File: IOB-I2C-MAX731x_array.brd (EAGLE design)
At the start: 108.7 x 112 mm, 30 parts, among them IC1X11 MAX7311, IC1X12 MAX7311, IC1X13 MAX7311, SW1X11 A0, SW1X12 A0, SW1X13 A0, SW2X11 A1, SW2X12 A1, SW2X13 A1, SW3X11 A2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

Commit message: cleanup layout
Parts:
- BOARDX11, BOARDX12, BOARDX13: value I2C-EXPANDER -> CONNECTOR-I2C-EXPANDER
- moved U$1X13 2.84 mm to (19.7, 75.1)
- moved U$1X11 2.84 mm to (19.7, 9.02)
- moved U$1X12 2.84 mm to (19.7, 42.0)
- moved IC1X12 1.27 mm to (48.3, 52.1)
- moved SW1X12 1.27 mm to (73.0, 41.9)
- moved SW2X12 1.27 mm to (54.0, 41.9)
- moved SW3X12 1.27 mm to (34.9, 41.9)
- moved IC1X11 1.27 mm to (48.3, 19.1)
- moved SW1X11 1.27 mm to (73.0, 8.89)
- moved SW2X11 1.27 mm to (54.0, 8.89)
- moved SW3X11 1.27 mm to (34.9, 8.89)
- moved IC1X13 1.27 mm to (48.3, 85.1)
- moved SW1X13 1.27 mm to (73.0, 74.9)
- moved SW2X13 1.27 mm to (54.0, 74.9)
- moved SW3X13 1.27 mm to (34.9, 74.9)
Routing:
- net VCCX13: track 10.8 -> 0.00 mm, vias 2 -> 0
- net VCCX12: track 10.8 -> 0.00 mm, vias 2 -> 0
- net VCCX11: track 10.8 -> 0.00 mm, vias 2 -> 0
- net P9X13: track 31.2 -> 32.5 mm
- net P8X13: track 31.5 -> 32.8 mm
- net P9X12: track 31.2 -> 32.5 mm
- net P7X11: track 29.6 -> 30.9 mm
- net P8X12: track 31.5 -> 32.8 mm
- net P11X11: track 24.5 -> 25.8 mm
- net P10X12: track 29.7 -> 31.0 mm
- net P8X11: track 31.5 -> 32.8 mm
- net P6X11: track 25.2 -> 26.4 mm
- net P5X11: track 23.7 -> 24.9 mm
- net P12X11: track 22.6 -> 23.9 mm
- net P10X11: track 29.7 -> 31.0 mm
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
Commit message: added values for connectors
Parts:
- FID-LR, FID-UL: value (none) -> FIDUCIAL
- U$5X1: value (none) -> 10x10
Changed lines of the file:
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@@
 <element name="SW3X13" library="SPCoast" package="EDG-04" value="A2" x="34.925" y="74.93" rot="R180"/>
 <element name="U$1X13" library="SPCoast" package="OSHW-LOGO-L" value="DOC-OSHW-LOGO-L" x="19.685" y="75.057"/>
-<element name="FID-LR" library="SPCoast" package="FIDUCIAL_1MM" value="" x="93.98" y="8.89"/>
-<element name="FID-UL" library="SPCoast" package="FIDUCIAL_1MM" value="" x="5.08" y="91.44" smashed="yes">
+<element name="FID-LR" library="SPCoast" package="FIDUCIAL_1MM" value="FIDUCIAL" x="93.98" y="8.89"/>
+<element name="FID-UL" library="SPCoast" package="FIDUCIAL_1MM" value="FIDUCIAL" x="5.08" y="91.44" smashed="yes">
 <attribute name="NAME" x="8.255" y="88.9" size="1.016" layer="25" rot="R180"/>
 </element>
-<element name="U$5X1" library="SPCoast" package="BOARD-TEMPLATE-IOB-I2C-3X1-ARRAY" value="" x="0" y="0"/>
+<element name="U$5X1" library="SPCoast" package="BOARD-TEMPLATE-IOB-I2C-3X1-ARRAY" value="10x10" x="0" y="0"/>
 </elements>
 <signals>

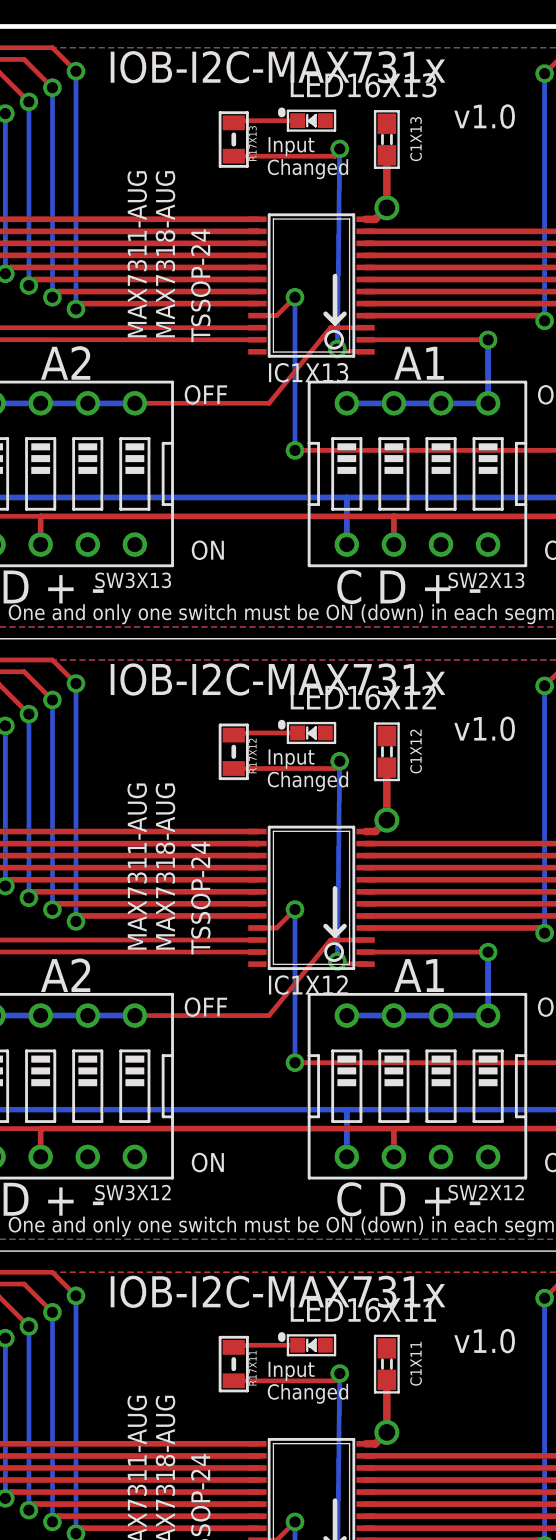
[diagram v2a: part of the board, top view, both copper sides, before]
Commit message: normalized values
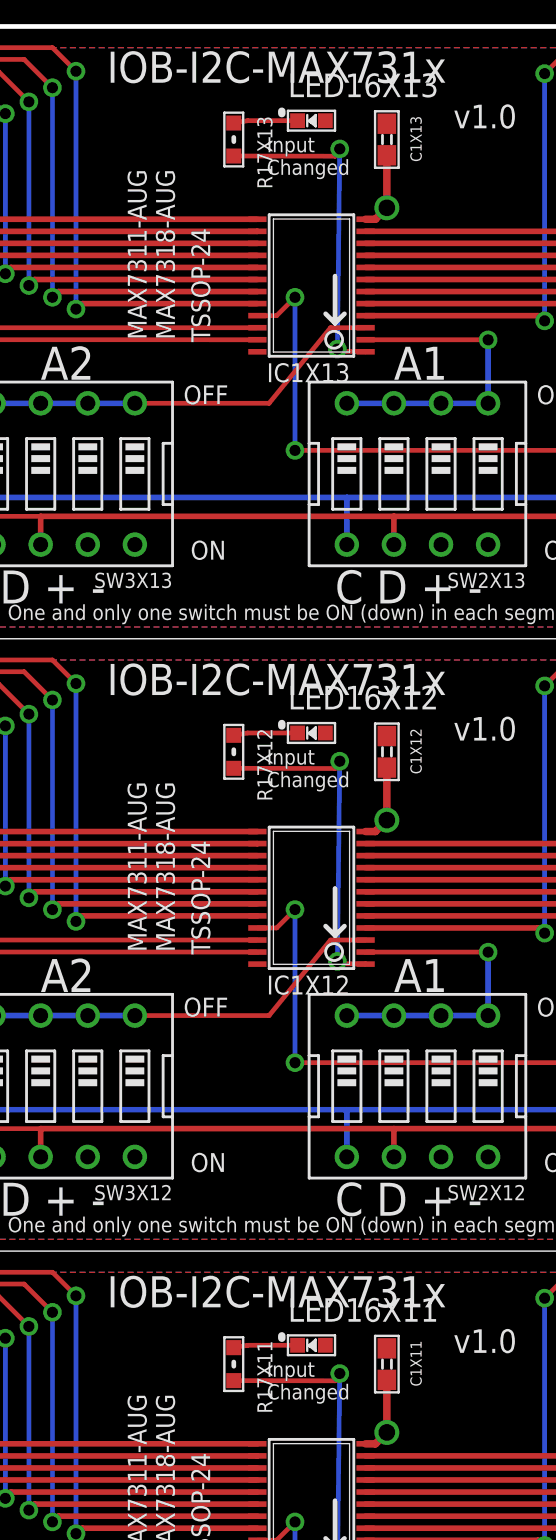
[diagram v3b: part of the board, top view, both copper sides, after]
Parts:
- R17X11, R17X12, R17X13: device SPCoast:0805-RES -> SPCoast:0603-RES
- SW1X11, SW1X12, SW1X13: value A0 -> SPSTx4
- SW2X11, SW2X12, SW2X13: value A1 -> SPSTx4
- SW3X11, SW3X12, SW3X13: value A2 -> SPSTx4
- U$5X1: value 10x10 -> BOARD
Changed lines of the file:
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@@
 <element name="IC1X11" library="SPCoast" package="TSSOP24" value="MAX7311" x="48.26" y="19.05" rot="R90"/>
 <element name="LED16X11" library="SPCoast" package="0603-LED" value="G" x="48.26" y="27.94"/>
-<element name="R17X11" library="SPCoast" package="0805-RES" value="4k7" x="44.069" y="26.924" rot="R270"/>
-<element name="SW1X11" library="SPCoast" package="EDG-04" value="A0" x="73.025" y="8.89" rot="R180"/>
-<element name="SW2X11" library="SPCoast" package="EDG-04" value="A1" x="53.975" y="8.89" rot="R180"/>
-<element name="SW3X11" library="SPCoast" package="EDG-04" value="A2" x="34.925" y="8.89" rot="R180"/>
+<element name="R17X11" library="SPCoast" package="0603-RES" value="4k7" x="44.069" y="26.924" rot="R270"/>
+<element name="SW1X11" library="SPCoast" package="EDG-04" value="SPSTx4" x="73.025" y="8.89" rot="R180"/>
+<element name="SW2X11" library="SPCoast" package="EDG-04" value="SPSTx4" x="53.975" y="8.89" rot="R180"/>
+<element name="SW3X11" library="SPCoast" package="EDG-04" value="SPSTx4" x="34.925" y="8.89" rot="R180"/>
 <element name="U$1X11" library="SPCoast" package="OSHW-LOGO-L" value="DOC-OSHW-LOGO-L" x="19.685" y="9.017"/>
 <element name="BOARDX12" library="SPCoast" package="I2C-EXPANDER" value="CONNECTOR-I2C-EXPANDER" x="48.26" y="60.96"/>
@@
 <element name="IC1X12" library="SPCoast" package="TSSOP24" value="MAX7311" x="48.26" y="52.07" rot="R90"/>
 <element name="LED16X12" library="SPCoast" package="0603-LED" value="G" x="48.26" y="60.96"/>
-<element name="R17X12" library="SPCoast" package="0805-RES" value="4k7" x="44.069" y="59.944" rot="R270"/>
-<element name="SW1X12" library="SPCoast" package="EDG-04" value="A0" x="73.025" y="41.91" rot="R180"/>
-<element name="SW2X12" library="SPCoast" package="EDG-04" value="A1" x="53.975" y="41.91" rot="R180"/>
-<element name="SW3X12" library="SPCoast" package="EDG-04" value="A2" x="34.925" y="41.91" rot="R180"/>
+<element name="R17X12" library="SPCoast" package="0603-RES" value="4k7" x="44.069" y="59.944" rot="R270"/>
+<element name="SW1X12" library="SPCoast" package="EDG-04" value="SPSTx4" x="73.025" y="41.91" rot="R180"/>
+<element name="SW2X12" library="SPCoast" package="EDG-04" value="SPSTx4" x="53.975" y="41.91" rot="R180"/>
+<element name="SW3X12" library="SPCoast" package="EDG-04" value="SPSTx4" x="34.925" y="41.91" rot="R180"/>
 <element name="U$1X12" library="SPCoast" package="OSHW-LOGO-L" value="DOC-OSHW-LOGO-L" x="19.685" y="42.037"/>
 <element name="BOARDX13" library="SPCoast" package="I2C-EXPANDER" value="CONNECTOR-I2C-EXPANDER" x="48.26" y="93.98"/>
@@
 <element name="IC1X13" library="SPCoast" package="TSSOP24" value="MAX7311" x="48.26" y="85.09" rot="R90"/>
 <element name="LED16X13" library="SPCoast" package="0603-LED" value="G" x="48.26" y="93.98"/>
-<element name="R17X13" library="SPCoast" package="0805-RES" value="4k7" x="44.069" y="92.964" rot="R270"/>
-<element name="SW1X13" library="SPCoast" package="EDG-04" value="A0" x="73.025" y="74.93" rot="R180"/>
-<element name="SW2X13" library="SPCoast" package="EDG-04" value="A1" x="53.975" y="74.93" rot="R180"/>
-<element name="SW3X13" library="SPCoast" package="EDG-04" value="A2" x="34.925" y="74.93" rot="R180"/>
+<element name="R17X13" library="SPCoast" package="0603-RES" value="4k7" x="44.069" y="92.964" rot="R270"/>
+<element name="SW1X13" library="SPCoast" package="EDG-04" value="SPSTx4" x="73.025" y="74.93" rot="R180"/>
+<element name="SW2X13" library="SPCoast" package="EDG-04" value="SPSTx4" x="53.975" y="74.93" rot="R180"/>
+<element name="SW3X13" library="SPCoast" package="EDG-04" value="SPSTx4" x="34.925" y="74.93" rot="R180"/>
 <element name="U$1X13" library="SPCoast" package="OSHW-LOGO-L" value="DOC-OSHW-LOGO-L" x="19.685" y="75.057"/>
 <element name="FID-LR" library="SPCoast" package="FIDUCIAL_1MM" value="FIDUCIAL" x="93.98" y="8.89"/>
@@
 <attribute name="NAME" x="8.255" y="88.9" size="1.016" layer="25" rot="R180"/>
 </element>
-<element name="U$5X1" library="SPCoast" package="BOARD-TEMPLATE-IOB-I2C-3X1-ARRAY" value="10x10" x="0" y="0"/>
+<element name="U$5X1" library="SPCoast" package="BOARD-TEMPLATE-IOB-I2C-3X1-ARRAY" value="BOARD" x="0" y="0"/>
 </elements>
 <signals>
@@
 <wire x1="50.038" y1="15.494" x2="51.1968" y2="15.494" width="0.254" layer="1"/>
 <wire x1="51.1968" y1="15.494" x2="51.1778" y2="15.475" width="0.254" layer="1"/>
-<wire x1="44.069" y1="26.024" x2="49.541" y2="26.024" width="0.254" layer="1"/>
+<wire x1="44.069" y1="26.035" x2="49.541" y2="26.024" width="0.254" layer="1"/>
 <wire x1="49.541" y1="26.024" x2="49.784" y2="26.416" width="0.254" layer="1"/>
 <contactref element="R17X11" pad="2"/>
@@
 <signal name="N$38X11">
 <wire x1="47.51" y1="27.94" x2="44.82" y2="27.94" width="0.254" layer="1"/>
-<wire x1="44.82" y1="27.94" x2="44.069" y2="27.824" width="0.254" layer="1"/>
+<wire x1="44.82" y1="27.94" x2="44.069" y2="27.813" width="0.254" layer="1"/>
 <contactref element="LED16X11" pad="C"/>
 <contactref element="R17X11" pad="1"/>
@@
 <wire x1="50.038" y1="48.514" x2="51.1968" y2="48.514" width="0.254" layer="1"/>
 <wire x1="51.1968" y1="48.514" x2="51.1778" y2="48.495" width="0.254" layer="1"/>
-<wire x1="44.069" y1="59.044" x2="49.541" y2="59.044" width="0.254" layer="1"/>
+<wire x1="44.069" y1="59.055" x2="49.541" y2="59.044" width="0.254" layer="1"/>
 <wire x1="49.541" y1="59.044" x2="49.784" y2="59.436" width="0.254" layer="1"/>
 <contactref element="R17X12" pad="2"/>
@@
 <signal name="N$38X12">
 <wire x1="47.51" y1="60.96" x2="44.82" y2="60.96" width="0.254" layer="1"/>
-<wire x1="44.82" y1="60.96" x2="44.069" y2="60.844" width="0.254" layer="1"/>
+<wire x1="44.82" y1="60.96" x2="44.069" y2="60.833" width="0.254" layer="1"/>
 <contactref element="LED16X12" pad="C"/>
 <contactref element="R17X12" pad="1"/>
@@
 <wire x1="50.038" y1="81.534" x2="51.1968" y2="81.534" width="0.254" layer="1"/>
 <wire x1="51.1968" y1="81.534" x2="51.1778" y2="81.515" width="0.254" layer="1"/>
-<wire x1="44.069" y1="92.064" x2="49.541" y2="92.064" width="0.254" layer="1"/>
+<wire x1="44.069" y1="92.075" x2="49.541" y2="92.064" width="0.254" layer="1"/>
 <wire x1="49.541" y1="92.064" x2="49.784" y2="92.456" width="0.254" layer="1"/>
 <contactref element="R17X13" pad="2"/>
@@
 <signal name="N$38X13">
 <wire x1="47.51" y1="93.98" x2="44.82" y2="93.98" width="0.254" layer="1"/>
-<wire x1="44.82" y1="93.98" x2="44.069" y2="93.864" width="0.254" layer="1"/>
+<wire x1="44.82" y1="93.98" x2="44.069" y2="93.853" width="0.254" layer="1"/>
 <contactref element="LED16X13" pad="C"/>
 <contactref element="R17X13" pad="1"/>
